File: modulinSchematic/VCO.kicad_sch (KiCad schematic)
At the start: 0 parts

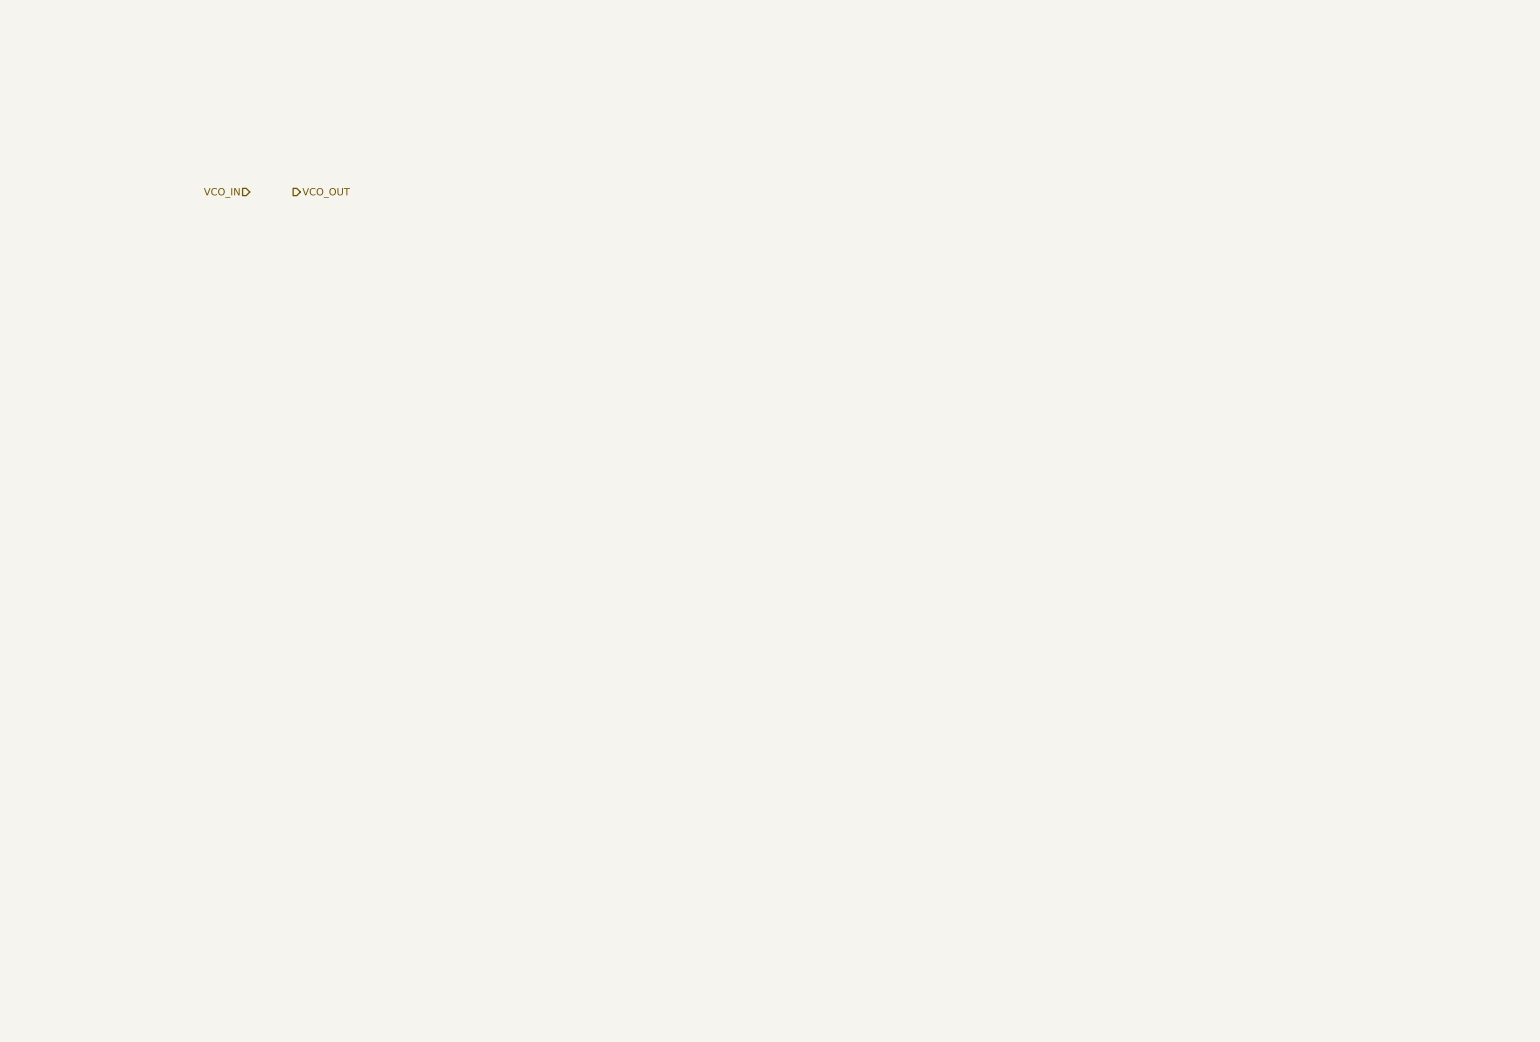
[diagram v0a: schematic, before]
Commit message: Add power schematic
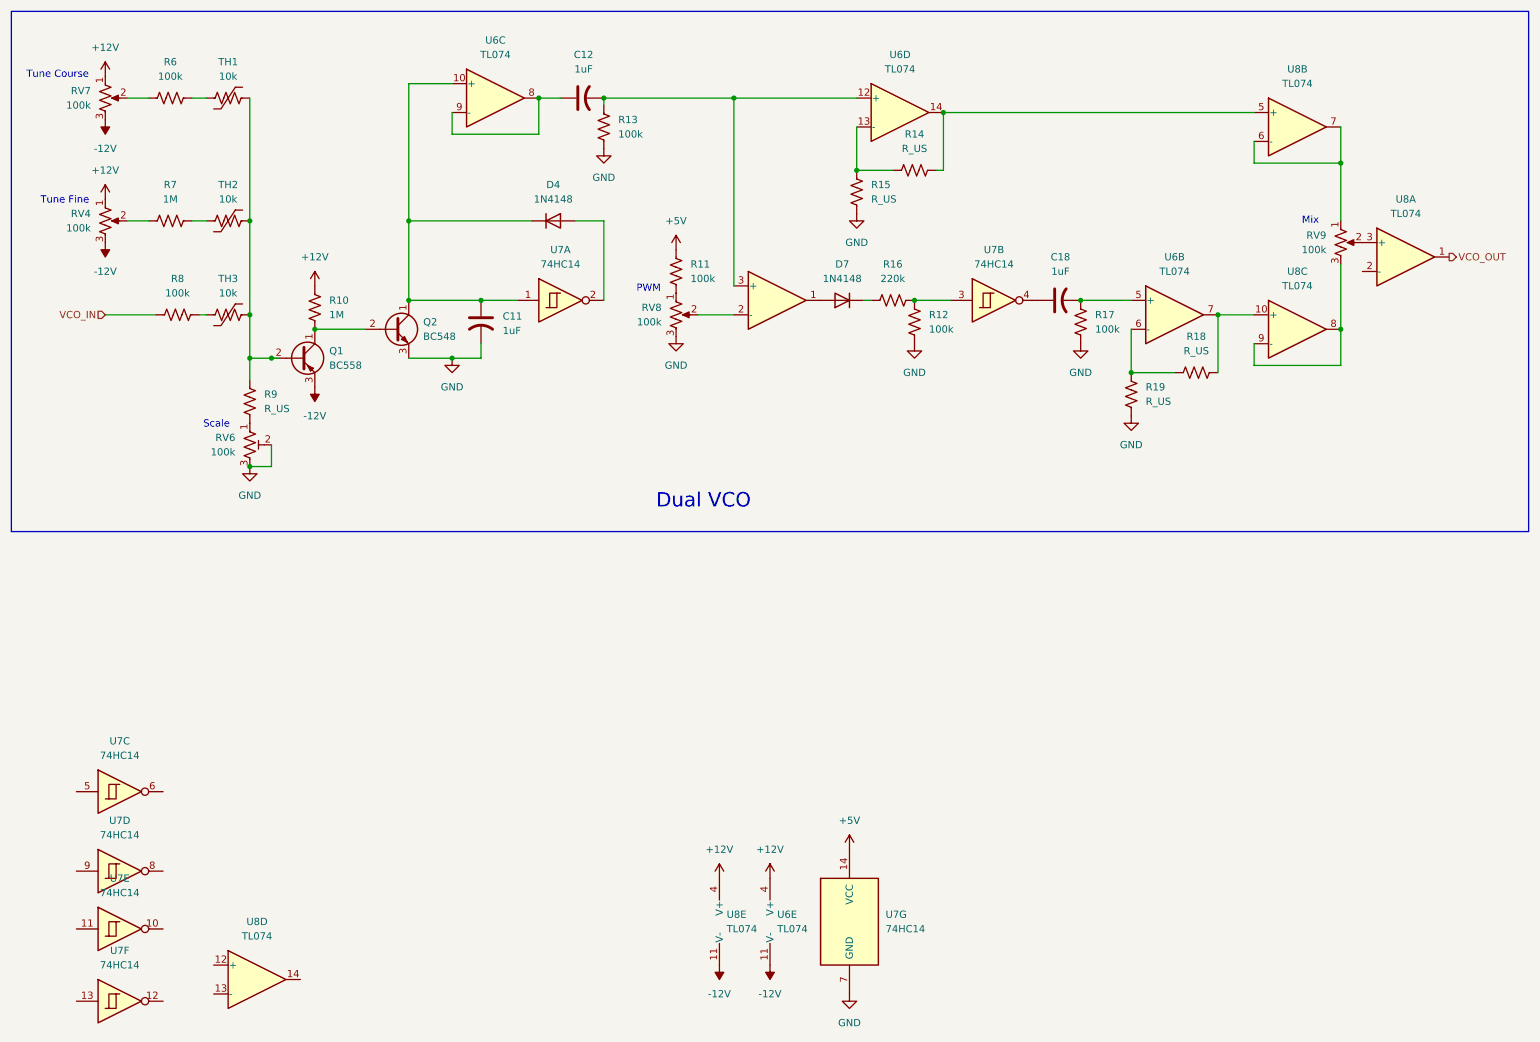
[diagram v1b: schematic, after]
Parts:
- added C11, C12, C18: 1uF, Capacitor_THT:CP_Radial_D4.0mm_P2.00mm, symbol Device:C_US
- added D4, D7: 1N4148, Diode_THT:D_DO-35_SOD27_P7.62mm_Horizontal, symbol Diode:1N4148
- added Q1: BC558, Package_TO_SOT_THT:TO-92_Inline, symbol Transistor_BJT:BC558
- added Q2: BC548, Package_TO_SOT_THT:TO-92_Inline, symbol Transistor_BJT:BC548
- added R10, R7: 1M, Resistor_THT:R_Axial_DIN0207_L6.3mm_D2.5mm_P10.16mm_Horizontal, symbol Device:R_US
- added R11, R12, R13, R17, R6, R8: 100k, Resistor_THT:R_Axial_DIN0207_L6.3mm_D2.5mm_P10.16mm_Horizontal, symbol Device:R_US
- added R14, R15, R18, R19, R9: R_US, Resistor_THT:R_Axial_DIN0207_L6.3mm_D2.5mm_P10.16mm_Horizontal, symbol Device:R_US
- added R16: 220k, Resistor_THT:R_Axial_DIN0207_L6.3mm_D2.5mm_P10.16mm_Horizontal, symbol Device:R_US
- added RV4, RV7, RV8, RV9: 100k, Potentiometer_THT:Potentiometer_Alpha_RD901F-40-00D_Single_Vertical, symbol Device:R_Potentiometer_US
- added RV6: 100k, Potentiometer_THT:Potentiometer_Bourns_3266Y_Vertical, symbol Device:R_Potentiometer_Trim_US
- added TH1, TH2, TH3: 10k, symbol Device:Thermistor_US
- added U6, U8: TL074, Package_DIP:DIP-14_W7.62mm, symbol Amplifier_Operational:TL074
- added U7: 74HC14, symbol 74xx:74HC14
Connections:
- net VCO_IN: now also R8.1
- net VCO_OUT: now also U8.1
- new net: R9.1, RV6.1
- new net: R12.2, R16.1, U7.3
- new net: C18.1, U7.4
- new net: C11.1, D4.1 (K), Q2.1 (C), U6.10 (+), U7.1
- new net: D4.2 (A), U7.2
- new net: RV9.1, U8.6 (-), U8.7
- new net: RV9.2, U8.3 (+)
- new net: RV9.3, U8.8, U8.9 (-)
- new net: D7.1 (K), R16.2
- new net: D7.2 (A), U6.1
- new net: C12.1, U6.8, U6.9 (-)
- new net: Q1.1 (C), Q2.2 (B), R10.1
- new net: C12.2, R13.1, U6.12 (+), U6.3 (+)
- new net: R7.1, RV4.2
- new net: R7.2, TH2.1
- new net: C18.2, R17.1, U6.5 (+)
- new net: R18.1, R19.1, U6.6 (-)
- new net: R18.2, U6.7, U8.10 (+)
- new net: R14.2, R15.1, U6.13 (-)
- new net: R14.1, U6.14, U8.5 (+)
- new net: R6.1, RV7.2
- new net: R6.2, TH1.1
- new net: Q1.2 (B), R9.2, TH1.2, TH2.2, TH3.2
- new net: R8.2, TH3.1
- new net: R11.1, RV8.1
- new net: RV8.2, U6.2 (-)
- new net +12V: R10.2, RV4.1, RV7.1, U6.4 (V+), U8.4 (V+)
- new net +5V: R11.2, U7.14 (VCC)
- new net -12V: Q1.3 (E), RV4.3, RV7.3, U6.11 (V-), U8.11 (V-)
- new net GND: C11.2, Q2.3 (E), R12.1, R13.2, R15.2, R17.2, R19.2, RV6.2, RV6.3, RV8.3, U7.7 (GND)
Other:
- note added: "Dual VCO"
- note added: "Mix"
- note added: "PWM"
- note added: "Scale"
- note added: "Tune Course"
- note added: "Tune Fine"

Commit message: Create Power supply PCB
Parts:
- R9: value R_US -> 1k
- RV6: value 100k -> 1k
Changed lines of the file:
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@@
 			)
 		)
-		(property "Value" "100k"
+		(property "Value" "1k"
 			(at 54.61 92.7099 0)
 			(effects
@@
 			)
 		)
-		(property "Value" "R_US"
+		(property "Value" "1k"
 			(at 59.69 85.0899 0)
 			(effects

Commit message: Start OCB design for parts
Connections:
- net VCO_OUT: now also U8.2 (-)
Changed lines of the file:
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@@
+	(wire
+		(pts
+			(xy 267.97 64.77) (xy 267.97 58.42)
+		)
+		(stroke
+			(width 0)
+			(type default)
+		)
+	)
 	(wire
 		(pts
@@
 	(wire
 		(pts
+			(xy 252.73 64.77) (xy 267.97 64.77)
+		)
+		(stroke
+			(width 0)
+			(type default)
+		)
+	)
+	(wire
+		(pts
 			(xy 39.37 30.48) (xy 35.56 30.48)
 		)
@@
 		)
 		(stroke
+			(width 0)
+			(type default)
+		)
+	)
+	(wire
+		(pts
+			(xy 252.73 60.96) (xy 252.73 64.77)
+		)
+		(stroke
